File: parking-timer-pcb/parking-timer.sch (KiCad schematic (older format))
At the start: 31 parts, among them J1 Conn_01x02, J2 Conn_02x04_Odd_Even, J3 Conn_01x04, J4 Conn_01x11, J5 Conn_01x02, J6 Conn_01x04, Q1 AO3401A, U1 RDA5807M_Module, U2 STM8L101F3P6TR, U3 ADS1220xPW

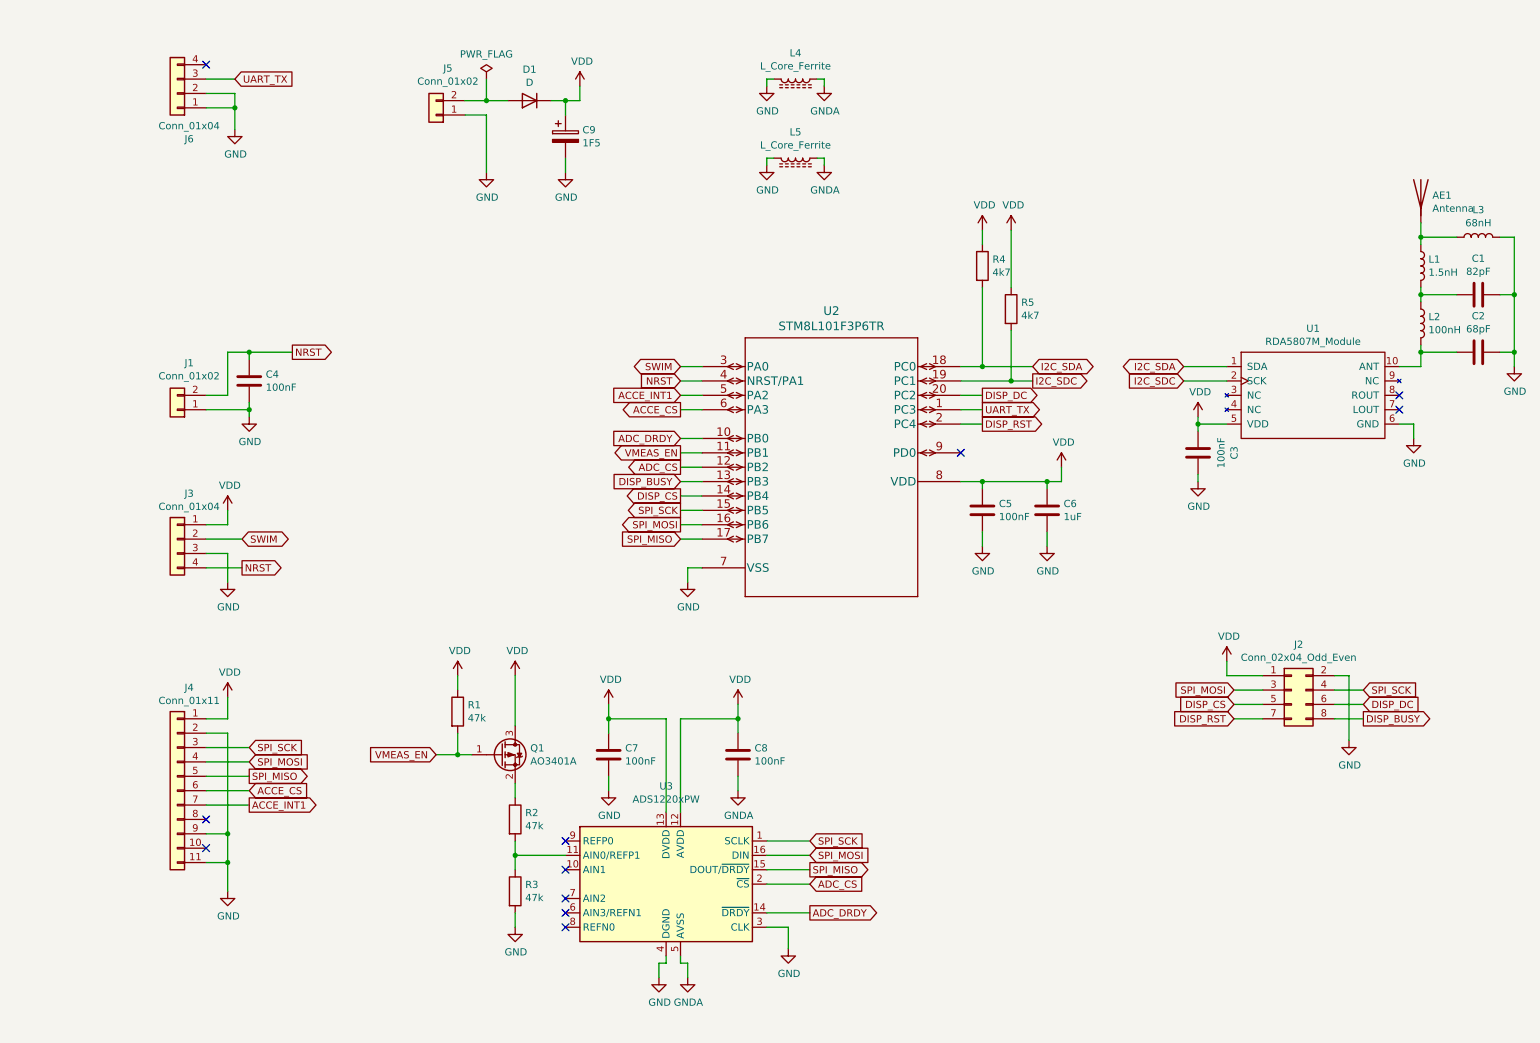
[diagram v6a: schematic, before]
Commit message: Parking-timer-pcg: Add debug GND pin. Add comments and reorganize a bit.
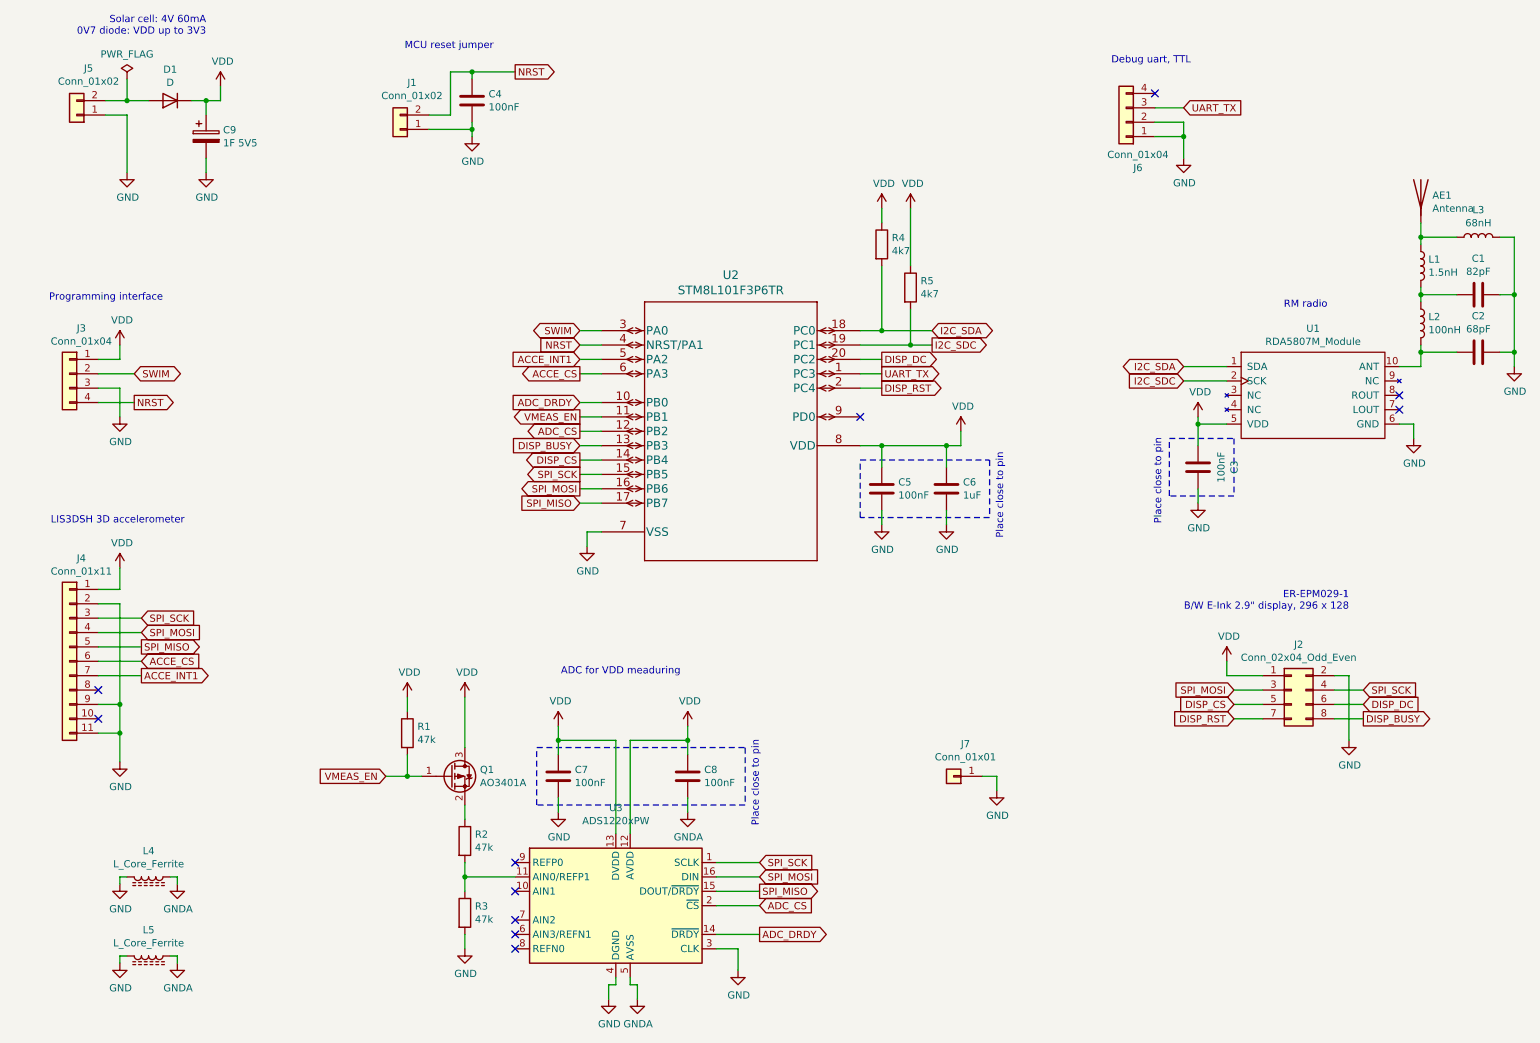
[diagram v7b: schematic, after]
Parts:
- added J7: Conn_01x01, Connector_PinHeader_2.54mm:PinHeader_1x01_P2.54mm_Vertical, symbol Connector_Generic:Conn_01x01
- C9: value 1F5 -> 1F 5V5
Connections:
- net GND: now also J7.1 (Pin_1)
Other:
- note added: "ADC for VDD meaduring"
- note added: "Debug uart, TTL"
- note added: "ER-EPM029-1\nB/W E-Ink 2.9" display, 296 x 128"
- note added: "LIS3DSH 3D accelerometer"
- note added: "MCU reset jumper"
- note added: "Place close to pin"
- note added: "Programming interface"
- note added: "RM radio"
- note added: "Solar cell: 4V 60mA\n0V7 diode: VDD up to 3V3"
- moved on the sheet: C3, C4, C5, C6, C7, C8, C9, D1, J1, J3, J4, J5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
